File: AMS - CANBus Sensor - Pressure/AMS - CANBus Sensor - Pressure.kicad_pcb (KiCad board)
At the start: 4 copper layers, 50.4 x 49.6 mm, 30 parts, among them IC1 ATMEGA328PB-ANR, J1 ICSP, J2 TTL_Programmer, J3 Conn_02x10_Odd_Even, J4 Conn_01x02, J5 Power_And_CAN, Q1 IRF9Z34NPBF, U2 178.6165.0001, U3 MCP2551-I-SN, U4 MCP2515-xSO, Y1 16MHz, Y2 16MHz

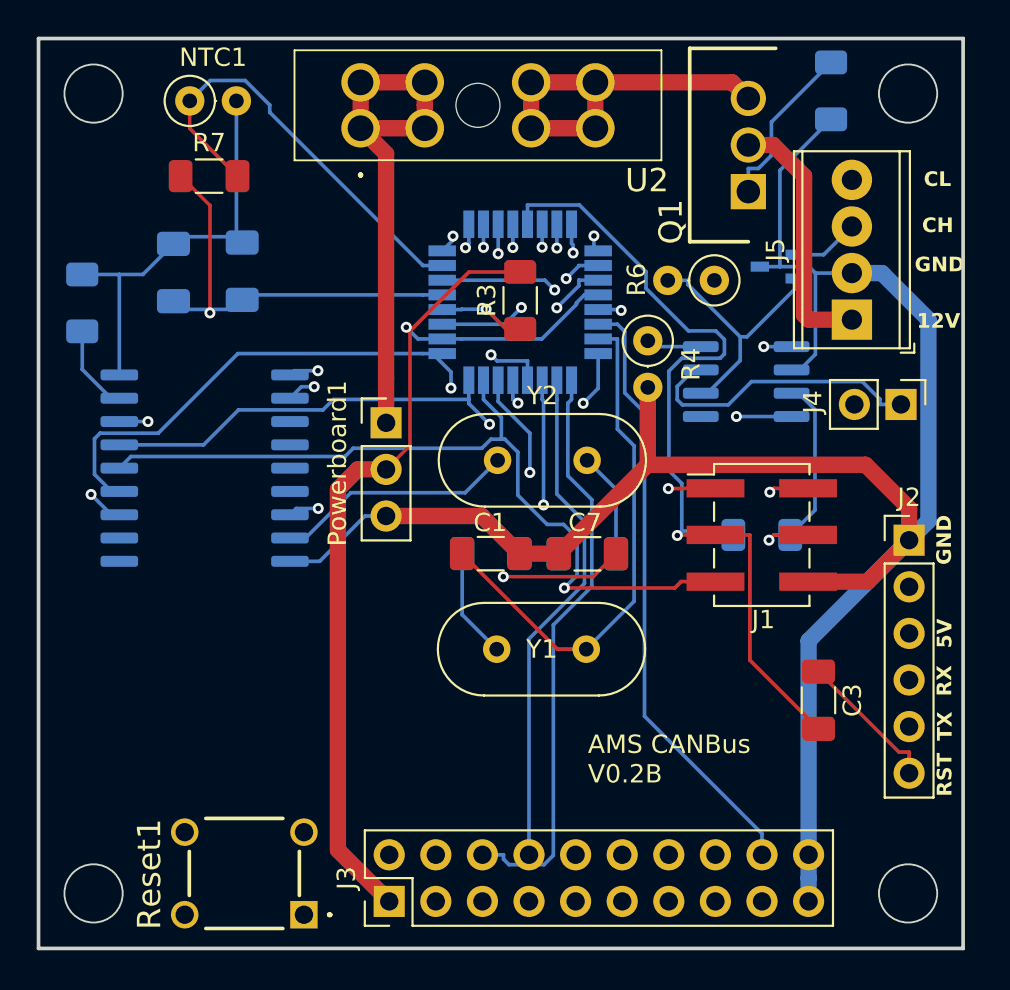
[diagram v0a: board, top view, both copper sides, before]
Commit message: working on the SMD version Making The Pressure version based off of the DIP Package
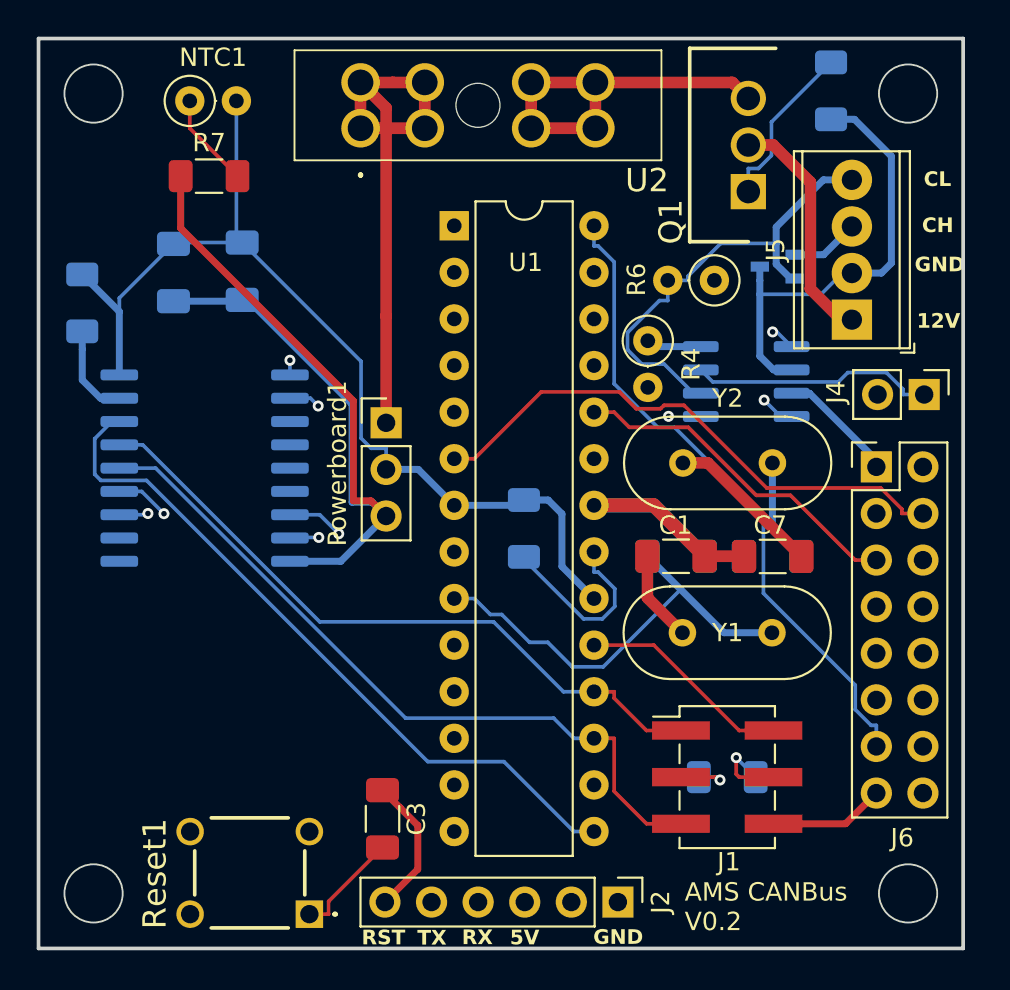
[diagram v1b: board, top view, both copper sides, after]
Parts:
- removed IC1: ATMEGA328PB-ANR, SamacSys_Parts:QFP80P900X900X120-32N
- removed J3: Conn_02x10_Odd_Even, Connector_PinHeader_2.54mm:PinHeader_2x10_P2.54mm_Vertical
- added J6: Conn_02x08_Odd_Even, Connector_PinHeader_2.54mm:PinHeader_2x08_P2.54mm_Vertical, F.Cu at (145.7, 73.8)
- added U1: ATmega328P-P, Package_DIP:DIP-28_W7.62mm, F.Cu at (122.7, 60.6)
- R3: moved to B.Cu
- moved J2 25.3 mm to (131.6, 97.5), turned to -90 degrees
- moved C3 24.6 mm to (118.8, 92.9)
- moved J1 13.3 mm to (137.5, 90.7)
- moved R1 13.3 mm to (137.5, 90.7)
- moved R3 12.4 mm to (126.5, 77.1)
- moved Y1 10.2 mm to (135.1, 82.8)
- moved C2 10.1 mm to (134.8, 78.6)
- moved C6 10.1 mm to (140.0, 78.6)
- moved C7 10.1 mm to (140.0, 78.6)
- moved Y2 10.1 mm to (135.1, 73.5)
- moved C1 10.1 mm to (134.8, 78.6)
- moved J4 1.37 mm to (148.3, 69.8)
- moved Reset1 0.30 mm to (114.8, 98.1)
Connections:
- net /BareMinATMEGA328PB-ANR/PB3-D11-MOSI renamed /BareMinAtmel328P/PB3-D11-MOSI
- net /BareMinATMEGA328PB-ANR/PB4-D12-MISO renamed /BareMinAtmel328P/PB4-D12-MISO
- net /BareMinATMEGA328PB-ANR/PB5-D13-SCK renamed /BareMinAtmel328P/PB5-D13-SCK
- net /BareMinATMEGA328PB-ANR/PC0-A0 renamed /BareMinAtmel328P/PC0-A0
- net /BareMinATMEGA328PB-ANR/RESET renamed /BareMinAtmel328P/RESET
- C1 pad 1: Net-(IC1-(XTAL1/TOSC1)_PB6) -> Net-(U1-XTAL2/PB7)
- C2 pad 1: Net-(IC1-(XTAL2/TOSC2)_PB7) -> Net-(U1-XTAL1/PB6)
- J2 pad 4: /BareMinATMEGA328PB-ANR/PD0-RX -> /BareMinAtmel328P/PD0-RX
- J2 pad 5: /BareMinATMEGA328PB-ANR/PD1-TX -> /BareMinAtmel328P/PD1-TX
- R3 pad 1: /BareMinATMEGA328PB-ANR/AREF -> /BareMinAtmel328P/AREF
- U4 pad 12: /BareMinATMEGA328PB-ANR/PD2-D2 -> /BareMinAtmel328P/PD2-D2
- U4 pad 16: /BareMinATMEGA328PB-ANR/PB1-D9 -> /BareMinAtmel328P/PB1-D9
- Y1 pad 1: Net-(IC1-(XTAL2/TOSC2)_PB7) -> Net-(U1-XTAL2/PB7)
- Y1 pad 2: Net-(IC1-(XTAL1/TOSC1)_PB6) -> Net-(U1-XTAL1/PB6)
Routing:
- net /BareMinATMEGA328PB-ANR/PD3-D3: track 47.8 -> 0.00 mm, vias 1 -> 0
- net /BareMinATMEGA328PB-ANR/PD4-D4: track 44.5 -> 0.00 mm, vias 1 -> 0
- net /BareMinATMEGA328PB-ANR/PE3-A7: track 44.5 -> 0.00 mm, vias 1 -> 0
- net /BareMinATMEGA328PB-ANR/PC5-A5: track 42.2 -> 0.00 mm, vias 1 -> 0
- net /BareMinATMEGA328PB-ANR/PE2-A6: track 41.6 -> 0.00 mm, vias 1 -> 0
- net /BareMinATMEGA328PB-ANR/PC4-A4: track 41.6 -> 0.00 mm, vias 1 -> 0
- net /BareMinAtmel328P/PD0-RX: track 0.00 -> 41.1 mm
- net /BareMinATMEGA328PB-ANR/PC3-A3: track 40.5 -> 0.00 mm, vias 1 -> 0
- net /BareMinAtmel328P/PC4-A4-SDA: track 0.00 -> 40.0 mm
- net /BareMinATMEGA328PB-ANR/PC2-A2: track 39.5 -> 0.00 mm, vias 1 -> 0
- net /BareMinATMEGA328PB-ANR/PC1-A1: track 38.7 -> 0.00 mm, vias 1 -> 0
- net /BareMinAtmel328P/PB1-D9: track 0.00 -> 38.5 mm
- net /BareMinATMEGA328PB-ANR/PE0-SDA: track 36.4 -> 0.00 mm, vias 1 -> 0
- net /BareMinATMEGA328PB-ANR/PD2-D2: track 36.4 -> 0.00 mm, vias 2 -> 0
- net /BareMinAtmel328P/PD1-TX: track 0.00 -> 36.3 mm
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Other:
- board text added: "AMS CANBus V0.2"
- board text removed: "AMS CANBus V0.2B"

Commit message: wip for this trying to figure out if i want to go completely SMD with this or not.
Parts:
- added IC1: OPA4340UA, SamacSys_Parts:SOIC127P600X175-14N, F.Cu at (72.6, 79.4)
- added J3: TTL_Programmer, Connector_PinHeader_2.54mm:PinHeader_1x06_P2.54mm_Vertical, F.Cu at (81.1, 76.6)
- added R10: 47K, Resistor_SMD:R_1206_3216Metric_Pad1.30x1.75mm_HandSolder, F.Cu at (65.4, 82.5)
- added R11: 47K, Resistor_SMD:R_1206_3216Metric_Pad1.30x1.75mm_HandSolder, F.Cu at (65.4, 85.8)
- added R12: 47K, Resistor_SMD:R_1206_3216Metric_Pad1.30x1.75mm_HandSolder, F.Cu at (65.4, 89.1)
- added R13: 47K, Resistor_SMD:R_1206_3216Metric_Pad1.30x1.75mm_HandSolder, F.Cu at (65.4, 92.4)
- added R14: 100K, Resistor_SMD:R_1206_3216Metric_Pad1.30x1.75mm_HandSolder, F.Cu at (65.4, 95.6)
- added R15: 100K, Resistor_SMD:R_1206_3216Metric_Pad1.30x1.75mm_HandSolder, F.Cu at (65.4, 98.9)
- added R8: 100K, Resistor_SMD:R_1206_3216Metric_Pad1.30x1.75mm_HandSolder, F.Cu at (65.4, 75.9)
- added R9: 100K, Resistor_SMD:R_1206_3216Metric_Pad1.30x1.75mm_HandSolder, F.Cu at (65.4, 79.2)
- added RV1: R_Potentiometer_US, Potentiometer_THT:Potentiometer_Bourns_3296W_Vertical, F.Cu at (70.5, 49.7)
- added RV2: R_Potentiometer_US, Potentiometer_THT:Potentiometer_Bourns_3296W_Vertical, F.Cu at (70.5, 56.1)
- added RV3: R_Potentiometer_US, Potentiometer_THT:Potentiometer_Bourns_3296W_Vertical, F.Cu at (70.5, 62.6)
- added RV4: R_Potentiometer_US, Potentiometer_THT:Potentiometer_Bourns_3296W_Vertical, F.Cu at (70.5, 69.0)
- added U5: 3568, SamacSys_Parts:3568, F.Cu at (78.1, 53.1)
- C1, C6, C7: value 22pf -> 100nf
- C3, C4, C5: value 100nf -> 22pf
- J1: value ICSP -> Power_And_CAN; footprint Connector_PinHeader_2.54mm:PinHeader_2x03_P2.54mm_Vertical_SMD -> TerminalBlock_Phoenix:TerminalBlock_Phoenix_MPT-0,5-4-2.54_1x04_P2.54mm_Horizontal
- J2: value TTL_Programmer -> Power_And_CAN; footprint Connector_PinHeader_2.54mm:PinHeader_1x06_P2.54mm_Vertical -> TerminalBlock_Phoenix:TerminalBlock_Phoenix_MPT-0,5-4-2.54_1x04_P2.54mm_Horizontal
- J4: value Conn_01x02 -> ICSP; footprint Connector_PinHeader_2.54mm:PinHeader_1x02_P2.54mm_Vertical -> Connector_PinHeader_2.54mm:PinHeader_2x03_P2.54mm_Vertical_SMD
- J5: value Power_And_CAN -> Conn_01x02; footprint TerminalBlock_Phoenix:TerminalBlock_Phoenix_MPT-0,5-4-2.54_1x04_P2.54mm_Horizontal -> Connector_PinHeader_2.54mm:PinHeader_1x02_P2.54mm_Vertical
- J6: value Conn_02x08_Odd_Even -> Screw_Terminal_01x02; footprint Connector_PinHeader_2.54mm:PinHeader_2x08_P2.54mm_Vertical -> TerminalBlock_Phoenix:TerminalBlock_Phoenix_MPT-0,5-2-2.54_1x02_P2.54mm_Horizontal
- R2: value 10k -> 4.7k
- R3: value 4.7k -> 10k
- R4: value 17k -> 10k; footprint Resistor_THT:R_Axial_DIN0207_L6.3mm_D2.5mm_P2.54mm_Vertical -> Resistor_SMD:R_1206_3216Metric_Pad1.30x1.75mm_HandSolder
- R6: value 120 -> 17k
- R7: value 10k -> 120; footprint Resistor_SMD:R_1206_3216Metric_Pad1.30x1.75mm_HandSolder -> Resistor_THT:R_Axial_DIN0207_L6.3mm_D2.5mm_P2.54mm_Vertical
- U1: value ATmega328P-P -> 3568; footprint Package_DIP:DIP-28_W7.62mm -> SamacSys_Parts:3568
- U2: value 178.6165.0001 -> ATmega328P-P; footprint SamacSys_Parts:17861650001 -> Package_DIP:DIP-28_W7.62mm
- U3: value MCP2551-I-SN -> MCP2515-xSO; footprint Package_SO:SOIC-8_3.9x4.9mm_P1.27mm -> Package_SO:SOIC-18W_7.5x11.6mm_P1.27mm
- U4: value MCP2515-xSO -> MCP2551-I-SN; footprint Package_SO:SOIC-18W_7.5x11.6mm_P1.27mm -> Package_SO:SOIC-8_3.9x4.9mm_P1.27mm
- moved J6 16.3 mm to (161.2, 78.5)
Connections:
- C1 pad 1: Net-(U1-XTAL2/PB7) -> Net-(J3-Pin_6)
- C1 pad 2: GND -> /BareMinAtmel328P/RESET
- C2 pad 1: Net-(U1-XTAL1/PB6) -> Net-(U2-XTAL1/PB6)
- C3 pad 1: Net-(J2-Pin_6) -> Net-(U2-XTAL2/PB7)
- C3 pad 2: /BareMinAtmel328P/RESET -> GND
- C4 pad 1: +5V -> Net-(U3-OSC2)
- C5 pad 1: +5V -> Net-(U3-OSC1)
- C6 pad 1: Net-(U4-OSC2) -> +5V
- C7 pad 1: Net-(U4-OSC1) -> +5V
- J1 pad 1: /BareMinAtmel328P/PB4-D12-MISO -> Net-(J1-Pin_1)
- J1 pad 2: /BareMinAtmel328P/PB5-D13-SCK -> GND
- J1 pad 3: /BareMinAtmel328P/RESET -> CANBUS_H
- J1 pad 4: +5V -> CANBUS_L
- J2 pad 1: GND -> Net-(J2-Pin_1)
- J2 pad 2: unconnected-(J2-Pin_2-Pad2) -> Net-(J2-Pin_2)
- J2 pad 3: +5V -> Net-(J2-Pin_3)
- J2 pad 4: /BareMinAtmel328P/PD0-RX -> Net-(J2-Pin_4)
- J4 pad 1: CANBUS_H -> /BareMinAtmel328P/PB4-D12-MISO
- J4 pad 2: Net-(J4-Pin_2) -> /BareMinAtmel328P/PB5-D13-SCK
- J5 pad 1: Net-(J5-Pin_1) -> CANBUS_H
- J5 pad 2: GND -> Net-(J5-Pin_2)
- J6 pad 1: +5V -> /BareMinAtmel328P/PD3-D3
- Q1 pad 2: Net-(J5-Pin_1) -> Net-(J1-Pin_1)
- R1 pad 1: +5V -> Net-(Q1-Pad1)
- R1 pad 2: /BareMinAtmel328P/RESET -> GND
- R2 pad 1: Net-(Q1-Pad1) -> /BareMinAtmel328P/AREF
- R2 pad 2: GND -> +5V
- R3 pad 1: /BareMinAtmel328P/AREF -> GND
- R3 pad 2: +5V -> /BareMinAtmel328P/PC0-A0
- R4 pad 1: Net-(U3-Rs) -> +5V
- R4 pad 2: GND -> /BareMinAtmel328P/RESET
- R5 pad 1: Net-(U4-~{RESET}) -> Net-(U3-~{RESET})
- R6 pad 1: Net-(J4-Pin_2) -> Net-(U4-Rs)
- R6 pad 2: CANBUS_L -> GND
- R7 pad 1: GND -> Net-(J5-Pin_2)
- R7 pad 2: /BareMinAtmel328P/PC0-A0 -> CANBUS_L
- U1 pad 1: /BareMinAtmel328P/RESET -> /BareMinAtmel328P/PD3-D3
- U1 pad 2: /BareMinAtmel328P/PD0-RX -> /BareMinAtmel328P/PD3-D3
- U1 pad 3: /BareMinAtmel328P/PD1-TX -> +5V
- U1 pad 4: /BareMinAtmel328P/PD2-D2 -> +5V
- U2 pad 1: +VDC -> /BareMinAtmel328P/RESET
- U2 pad 2: +VDC -> /BareMinAtmel328P/PD0-RX
- U2 pad 3: Net-(Q1-Pad3) -> /BareMinAtmel328P/PD1-TX
- U2 pad 4: Net-(Q1-Pad3) -> /BareMinAtmel328P/PD2-D2
- U2 pad 5: Net-(Q1-Pad3) -> /BareMinAtmel328P/PD3-D3
- U2 pad 6: Net-(Q1-Pad3) -> /BareMinAtmel328P/PD4-D4
- U2 pad 7: +VDC -> +5V
- U2 pad 8: +VDC -> GND
- U3 pad 2: GND -> /CANBUS-MCP2515/RXtoCANTC
- U3 pad 3: +5V -> unconnected-(U3-CLKOUT/SOF-Pad3)
- U3 pad 4: /CANBUS-MCP2515/RXtoCANTC -> unconnected-(U3-~{TX0RTS}-Pad4)
- U3 pad 6: CANBUS_L -> unconnected-(U3-~{TX2RTS}-Pad6)
- U3 pad 7: CANBUS_H -> Net-(U3-OSC2)
- U3 pad 8: Net-(U3-Rs) -> Net-(U3-OSC1)
- U4 pad 2: /CANBUS-MCP2515/RXtoCANTC -> GND
- U4 pad 3: unconnected-(U4-CLKOUT/SOF-Pad3) -> +5V
- U4 pad 4: unconnected-(U4-~{TX0RTS}-Pad4) -> /CANBUS-MCP2515/RXtoCANTC
- U4 pad 6: unconnected-(U4-~{TX2RTS}-Pad6) -> CANBUS_L
- U4 pad 7: Net-(U4-OSC2) -> CANBUS_H
- U4 pad 8: Net-(U4-OSC1) -> Net-(U4-Rs)
- Y1 pad 1: Net-(U1-XTAL2/PB7) -> Net-(U2-XTAL2/PB7)
- Y1 pad 2: Net-(U1-XTAL1/PB6) -> Net-(U2-XTAL1/PB6)
- Y2 pad 1: Net-(U4-OSC1) -> Net-(U3-OSC1)
- Y2 pad 2: Net-(U4-OSC2) -> Net-(U3-OSC2)
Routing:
- net (no net): track 0.00 -> 101.0 mm
- net Net-(U4-OSC2): track 36.9 -> 0.00 mm, vias 1 -> 0
- net /BareMinAtmel328P/PD2-D2: track 21.6 -> 57.2 mm
- net /BareMinAtmel328P/PC5-A5-SCL: track 35.6 -> 0.00 mm
- net Net-(U4-OSC1): track 31.6 -> 0.00 mm, vias 1 -> 0
- net /BareMinAtmel328P/PD4-D4: track 30.1 -> 0.00 mm
- net /CANBUS-MCP2515/RXtoCANTC: track 29.9 -> 0.00 mm, vias 2 -> 0
- net /BareMinAtmel328P/PC0-A0: track 39.5 -> 69.4 mm, vias 0 -> 2
- net /BareMinAtmel328P/PD5-D5: track 28.7 -> 0.00 mm
- net /BareMinAtmel328P/PB2-D10-SS: track 18.9 -> 47.6 mm
- net /BareMinAtmel328P/PD3-D3: track 28.2 -> 0.00 mm
- net GND: track 192.8 -> 218.8 mm
- net Net-(U2-XTAL1/PB6): track 0.00 -> 24.1 mm
- net Net-(U1-XTAL1/PB6): track 24.1 -> 0.00 mm
- net /BareMinAtmel328P/AREF: track 10.2 -> 30.1 mm
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
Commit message: ready for fab
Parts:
- removed IC1: OPA4340UA, SamacSys_Parts:SOIC127P600X175-14N
- added IC2: OPA4340UA, SamacSys_Parts:SOIC127P600X175-14N, B.Cu at (120.5, 94.3)
- C1, C7, R14, R15, R4, R8, R9: moved to B.Cu
- C5: moved to F.Cu
- RV1, RV2, RV3, RV4: value R_Potentiometer_US -> 200k
- moved RV1 98.9 mm to (154.3, 102.3), turned to 180 degrees
- moved RV2 92.7 mm to (154.3, 95.9), turned to 180 degrees
- moved RV3 87.9 mm to (154.3, 89.4), turned to 180 degrees
- moved RV4 84.9 mm to (154.3, 83.0), turned to 180 degrees
- moved J3 78.7 mm to (146.3, 120.7), turned to -90 degrees
- moved C4 74.0 mm to (161.1, 114.0), turned to 180 degrees
- moved C5 71.4 mm to (161.1, 114.0), turned to 180 degrees
- moved U1 70.0 mm to (179.3, 101.8), turned to 180 degrees
- moved R8 68.6 mm to (129.0, 101.5), turned to 180 degrees
- moved R9 68.6 mm to (129.0, 104.8), turned to 180 degrees
- moved U5 59.3 mm to (135.0, 70.0), turned to 180 degrees
- moved R11 57.1 mm to (122.4, 82.6)
- moved R10 57.0 mm to (122.3, 78.9)
- moved U4 56.6 mm to (165.6, 72.3)
- moved R13 53.4 mm to (117.0, 78.9), turned to 180 degrees
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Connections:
- J6 pad 1: /BareMinAtmel328P/PD3-D3 -> Net-(J6-Pin_1)
- J6 pad 2: /BareMinAtmel328P/PD3-D3 -> Net-(J6-Pin_2)
- RV1 pad 1: Net-(J2-Pin_4) -> Net-(J2-Pin_1)
- RV1 pad 2: /BufferedADC/ADCIN4 -> /BufferedADC/ADCIN1
- RV2 pad 1: Net-(J2-Pin_3) -> Net-(J2-Pin_2)
- RV2 pad 2: /BufferedADC/ADCIN3 -> /BufferedADC/ADCIN2
- RV3 pad 1: Net-(J2-Pin_2) -> Net-(J2-Pin_3)
- RV3 pad 2: /BufferedADC/ADCIN2 -> /BufferedADC/ADCIN3
- RV4 pad 1: Net-(J2-Pin_1) -> Net-(J2-Pin_4)
- RV4 pad 2: /BufferedADC/ADCIN1 -> /BufferedADC/ADCIN4
- U1 pad 1: /BareMinAtmel328P/PD3-D3 -> Net-(J6-Pin_2)
- U1 pad 2: /BareMinAtmel328P/PD3-D3 -> Net-(J6-Pin_1)
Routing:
- net (no net): track 101.0 -> 0.00 mm
- net /BufferedADC/ADCIN4: track 0.00 -> 98.9 mm, vias 0 -> 1
- net Net-(U3-OSC1): track 0.00 -> 77.0 mm, vias 1 -> 0
- net Net-(U3-OSC2): track 0.00 -> 72.5 mm, vias 1 -> 0
- net +5V: track 124.8 -> 185.4 mm, vias 1 -> 2
- net /BufferedADC/ADCIN3: track 0.00 -> 58.3 mm, vias 0 -> 1
- net /BareMinAtmel328P/PB3-D11-MOSI: track 40.3 -> 98.5 mm, vias 0 -> 1
- net GND: track 218.8 -> 276.6 mm, vias 0 -> 2
- net /BareMinAtmel328P/PB1-D9: track 38.5 -> 92.8 mm, vias 0 -> 2
- net /BareMinAtmel328P/PC0-A0: track 69.4 -> 15.9 mm, vias 2 -> 0
- net /BareMinAtmel328P/PB2-D10-SS: track 47.6 -> 0.00 mm
- net /BufferedADC/ADCIN2: track 0.00 -> 45.2 mm, vias 0 -> 2
- net +VDC: track 67.5 -> 22.7 mm
- net /BareMinAtmel328P/PC3-A3: track 35.5 -> 78.5 mm, vias 0 -> 2
- net /BufferedADC/ADCIN1: track 0.00 -> 40.8 mm, vias 0 -> 1
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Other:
- board size 50.4 x 49.6 mm -> 72.9 x 71.1 mm
- copper layers 4 -> 2
- board text added: "1 Amp 5V"
- board text added: "120 Ohm CAN Bus Resistor"
- board text added: "3 Amp"
- board text added: "ADC"
- board text added: "AMS CANBus Voltage V1.0 Rev A"
- board text added: "Fused"
- board text added: "In"
- board text added: "In 1"
- board text added: "In 2"
- board text added: "In 3"
- board text added: "In 4"
- board text added: "MISO"
- board text added: "MOSI"
- board text added: "RESET"
- board text added: "SCK"
- board text added: "VDC"
- board text removed: "AMS CANBus V0.2"

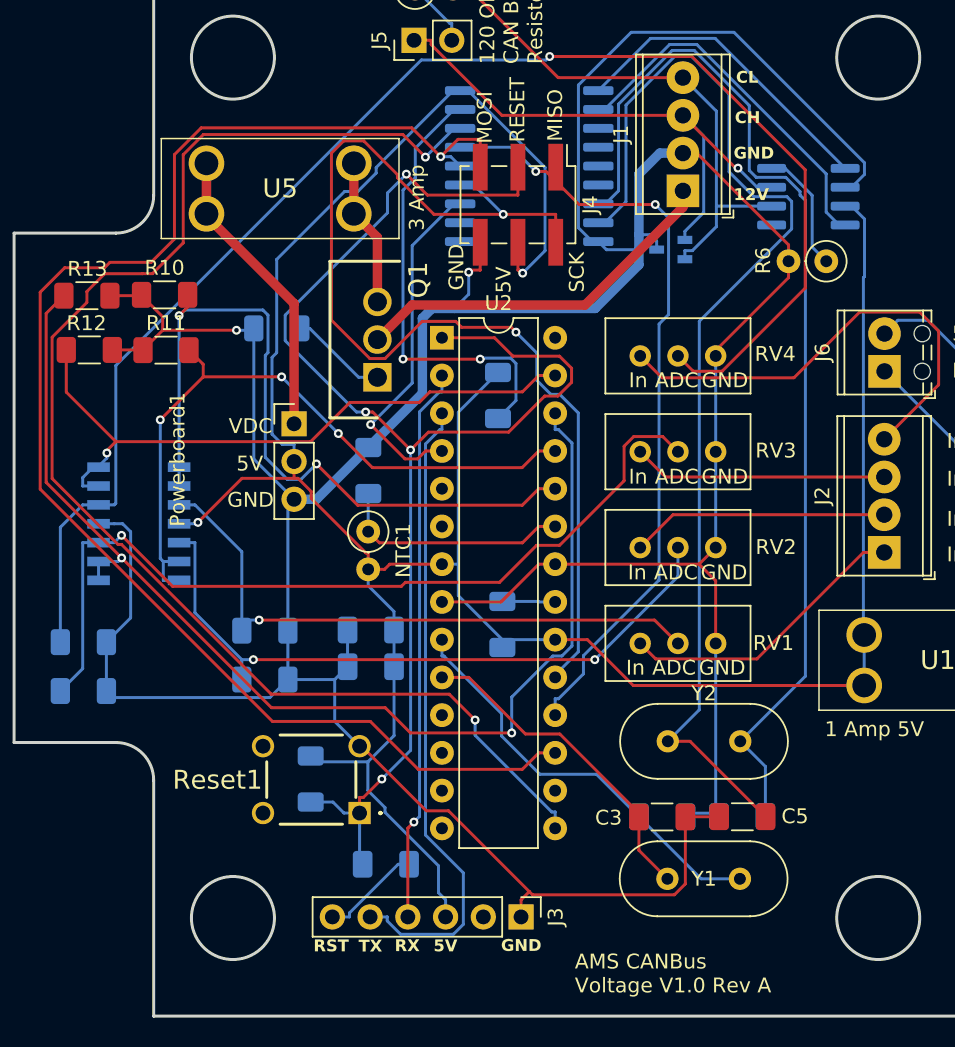
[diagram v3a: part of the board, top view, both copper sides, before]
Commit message: Pressure Sensor 1.0 Rev B boards. My dyslexic asss flipped the power pin out from the boards i have designed
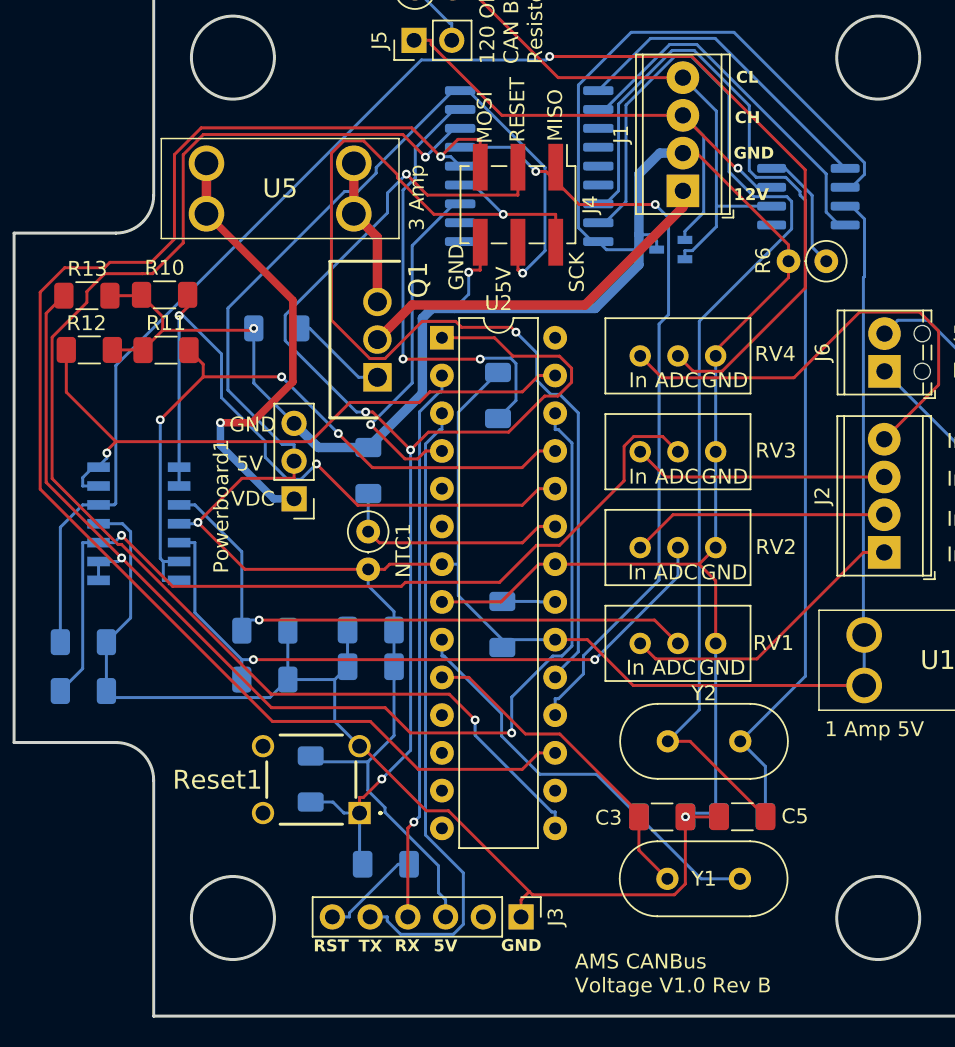
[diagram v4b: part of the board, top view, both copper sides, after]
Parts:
- moved Powerboard1 5.05 mm to (131.0, 92.6), turned to 180 degrees
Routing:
- net GND: track 276.6 -> 258.1 mm, vias 2 -> 3
- net +VDC: track 22.7 -> 32.4 mm, vias 0 -> 1
- net +5V: track 185.4 -> 189.5 mm
- net /BareMinAtmel328P/PC1-A1: track 51.2 -> 47.4 mm
- net Net-(Q1-Pad3): track 12.0 -> 10.3 mm
- net /BareMinAtmel328P/PB5-D13-SCK: track 75.2 -> 74.2 mm
- net /BareMinAtmel328P/PB4-D12-MISO: track 53.7 -> 52.8 mm
- net /CANBUS-MCP2515/RXtoCANTC: track 25.0 -> 24.1 mm
- net /BufferedADC/ADCIN1: track 40.8 -> 40.1 mm
- net /BufferedADC/ADCIN4: track 98.9 -> 98.3 mm
- net /BufferedADC/ADCIN3: track 58.3 -> 57.7 mm
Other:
- board text added: "AMS CANBus Voltage V1.0 Rev B"
- board text removed: "AMS CANBus Voltage V1.0 Rev A"
